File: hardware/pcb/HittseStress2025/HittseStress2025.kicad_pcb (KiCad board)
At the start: 2 copper layers, 152.4 x 63.5 mm, 11 parts, among them J1 Conn_01x02_Socket, J2 Conn_01x02_Socket, J3 SMA_conector_female, U1 MINIDCDCBOOST5V, U2 TTGO_T-Beam_T22_V1.1

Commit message: Updated to version 2025 for use with LilyGO T-Beam V1.2
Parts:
- removed J2: Conn_01x02_Socket, TerminalBlock_Phoenix:TerminalBlock_Phoenix_MPT-0,5-2-2.54_1x02_P2.54mm_Horizontal
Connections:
- U1 pad 1: /5V_U -> /3V3
- U2 pad 13: /5V_U -> /5V_I
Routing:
- net /3V3: track 92.9 -> 157.9 mm
- net /5V_U: track 37.8 -> 0.00 mm
- net /GND: track 258.7 -> 235.7 mm, vias 116 -> 117
- net /5V_I: track 72.7 -> 79.8 mm
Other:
- board text added: "Hittestress 2025"
- board text added: "version 3.1 (20251013)"
- board text removed: "Hittestress 2023"
- board text removed: "USB 5V"
- board text removed: "version 1.0 (20240108)"

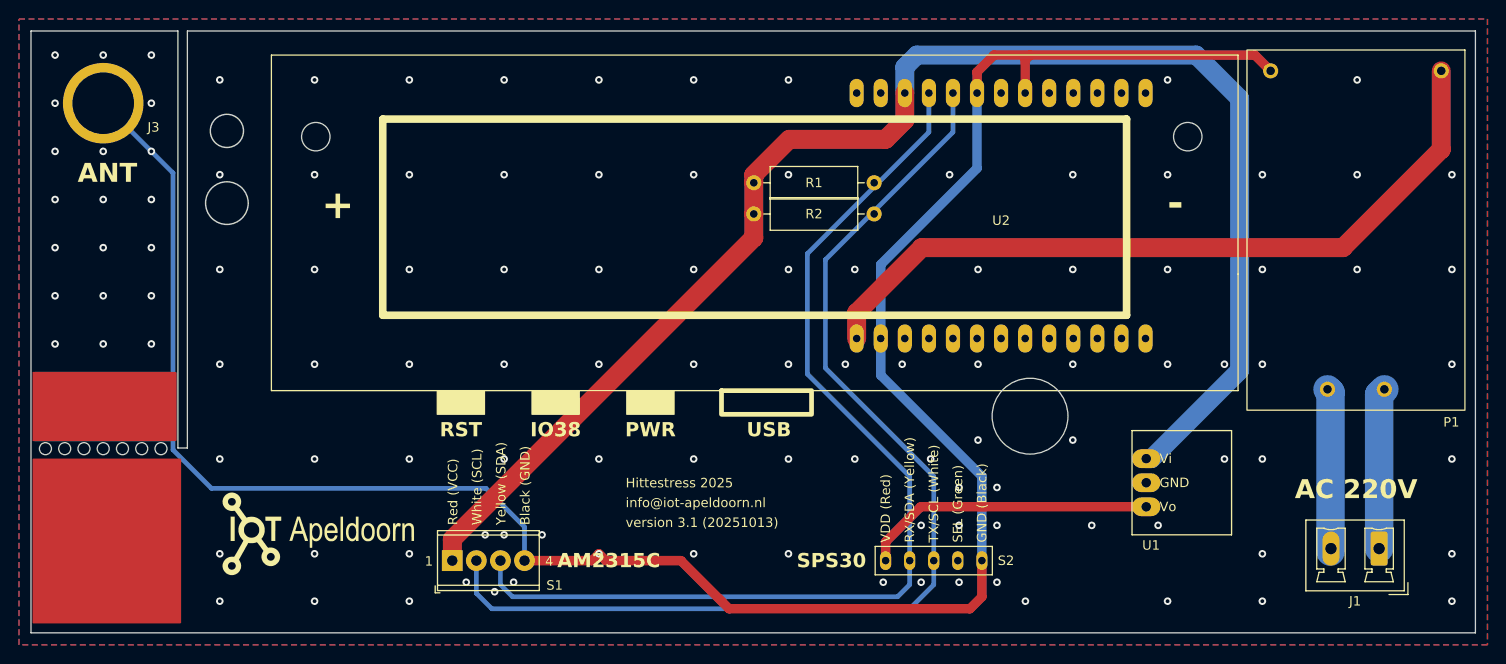
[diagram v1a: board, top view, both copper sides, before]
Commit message: Corrected position of components
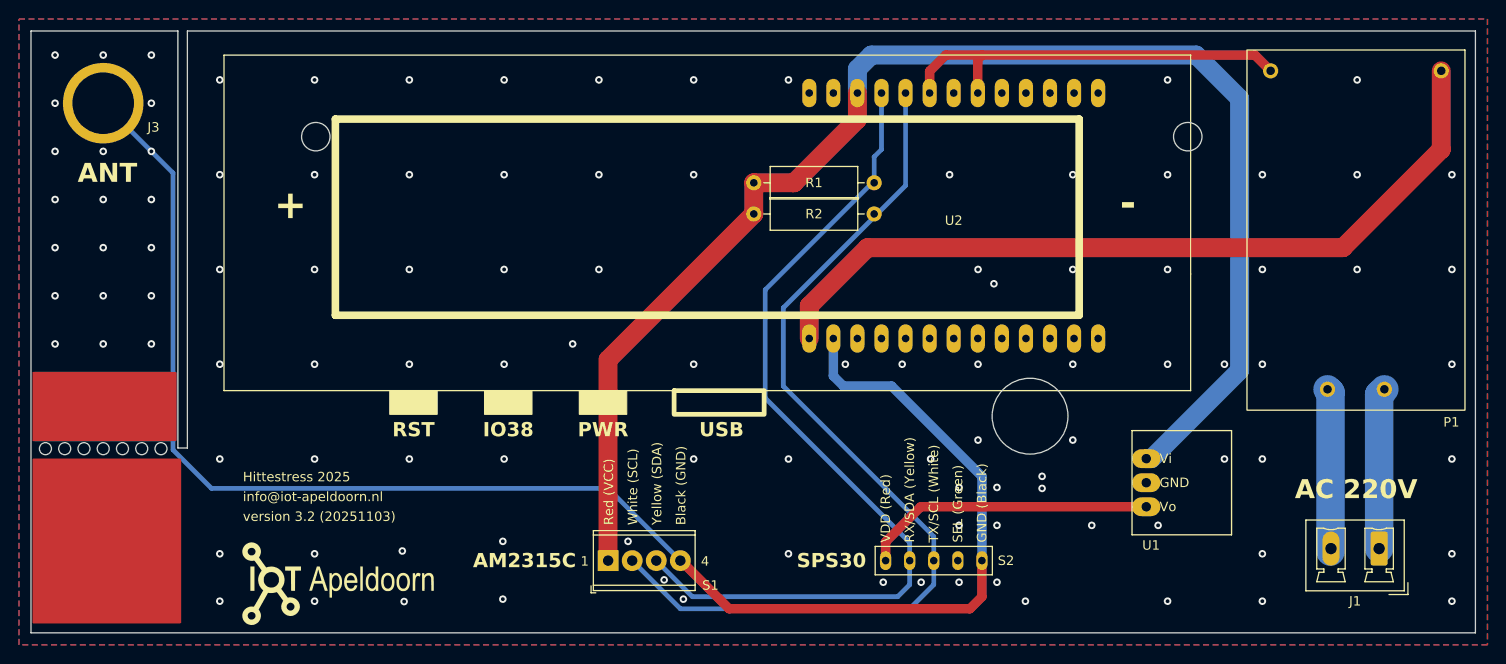
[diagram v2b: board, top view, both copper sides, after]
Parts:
- moved S1 16.4 mm to (139.7, 91.5)
- moved G*** 5.66 mm to (110.7, 94.0)
- moved U2 5.00 mm to (201.1, 73.5)
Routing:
- net /GND: track 235.7 -> 213.0 mm, vias 117 -> 109
- net /SCL: track 115.6 -> 99.0 mm
- net /SDA: track 108.4 -> 92.2 mm
- net /3V3: track 157.9 -> 150.5 mm
- net /5V_I: track 79.8 -> 85.2 mm
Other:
- outline, holes or cut-outs redrawn
- board text added: "version 3.2 (20251103)"
- board text removed: "version 3.1 (20251013)"
